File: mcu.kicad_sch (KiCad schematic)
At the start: 32 parts, among them U1 STM32H723VGTx, U13 BMI323, U14 AS5047P-ATST, U15 TCAN1044VDRQ1, X1 8MHz

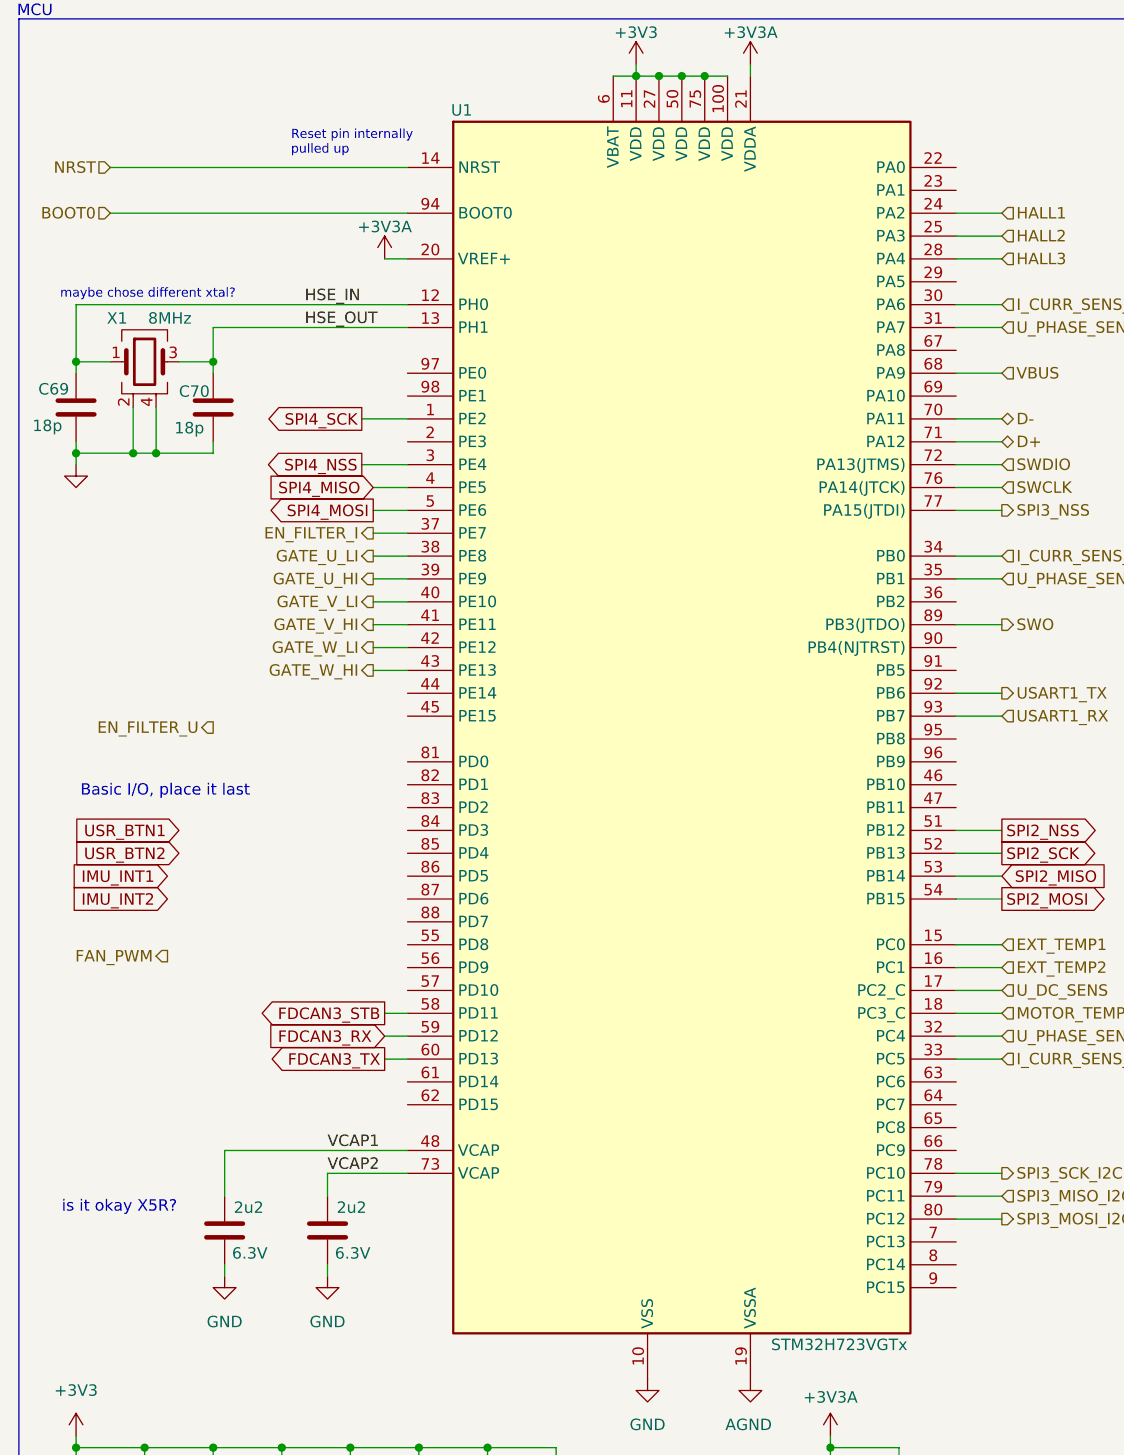
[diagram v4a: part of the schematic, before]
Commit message: added Net Classes  added +5V supply selection header
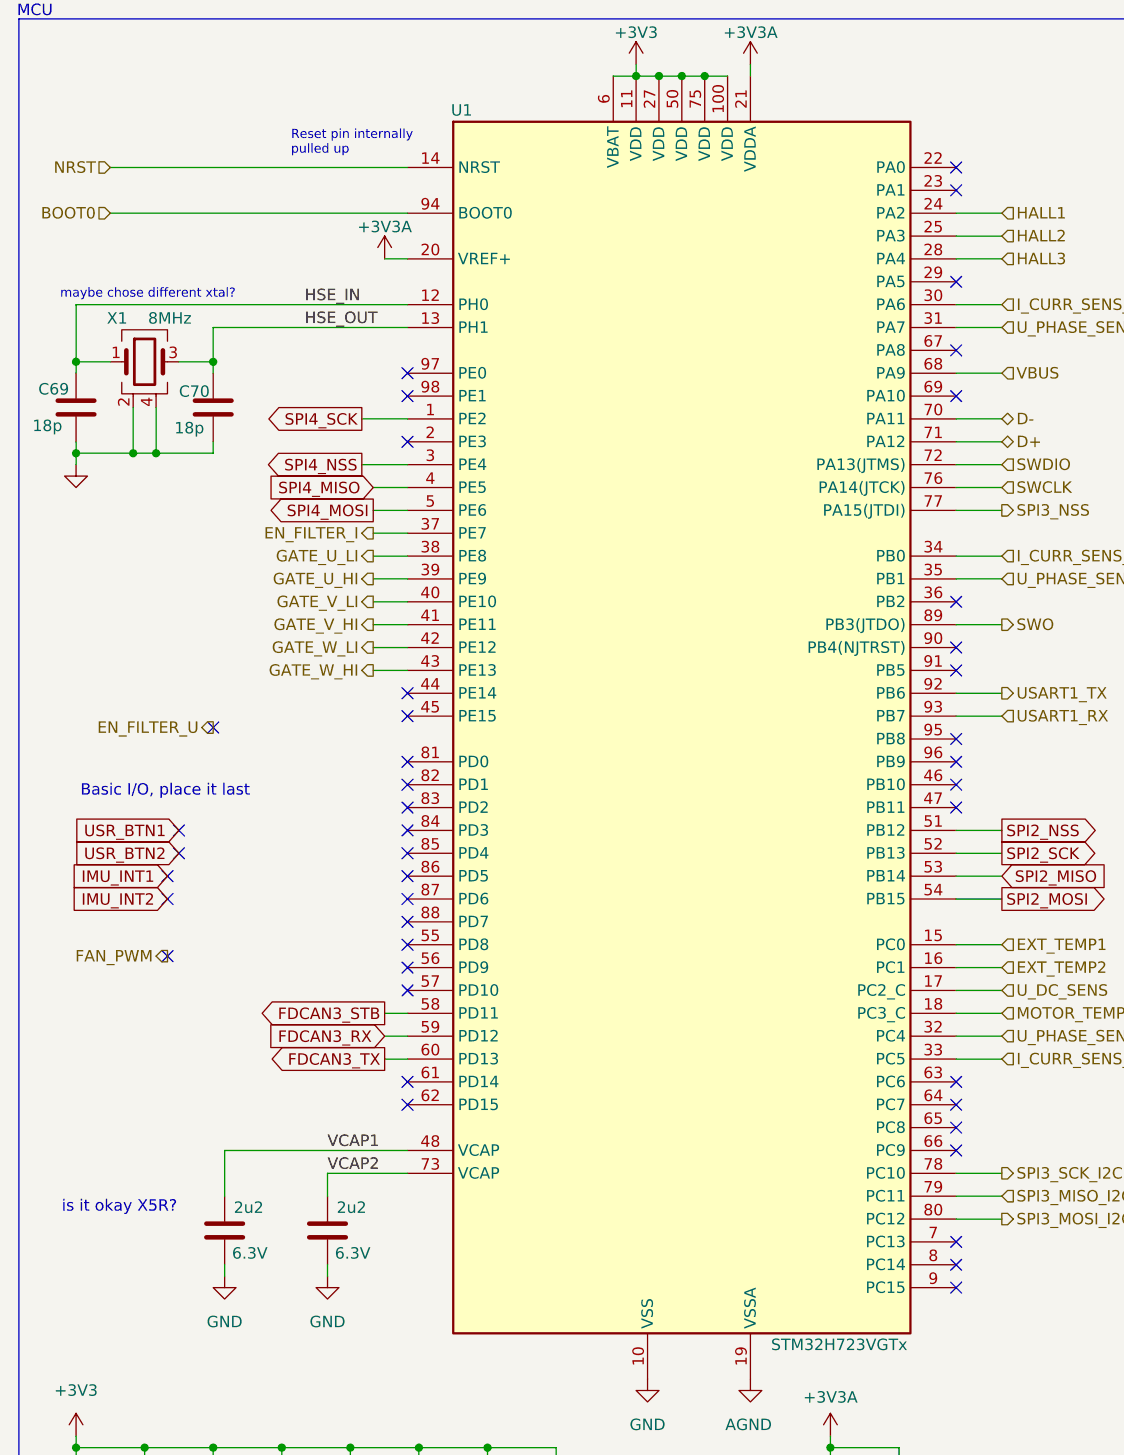
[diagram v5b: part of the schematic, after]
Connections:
- no-connect marks 6 -> 49
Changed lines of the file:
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@@
+	)
+	(no_connect
+		(at 116.84 85.09)
+	)
+	(no_connect
+		(at 116.84 97.79)
+	)
+	(no_connect
+		(at 116.84 133.35)
 	)
 	(no_connect
@@
 	)
 	(no_connect
+		(at 116.84 135.89)
+	)
+	(no_connect
+		(at 116.84 156.21)
+	)
+	(no_connect
+		(at 55.88 97.79)
+	)
+	(no_connect
+		(at 55.88 120.65)
+	)
+	(no_connect
+		(at 55.88 57.15)
+	)
+	(no_connect
+		(at 116.84 100.33)
+	)
+	(no_connect
+		(at 55.88 100.33)
+	)
+	(no_connect
+		(at 55.88 133.35)
+	)
+	(no_connect
+		(at 55.88 107.95)
+	)
+	(no_connect
+		(at 55.88 123.19)
+	)
+	(no_connect
+		(at 116.84 52.07)
+	)
+	(no_connect
 		(at 255.27 69.85)
+	)
+	(no_connect
+		(at 29.21 110.49)
+	)
+	(no_connect
+		(at 55.88 102.87)
+	)
+	(no_connect
+		(at 116.84 140.97)
 	)
 	(no_connect
@@
 	)
 	(no_connect
+		(at 116.84 153.67)
+	)
+	(no_connect
+		(at 55.88 92.71)
+	)
+	(no_connect
+		(at 116.84 95.25)
+	)
+	(no_connect
+		(at 30.48 105.41)
+	)
+	(no_connect
+		(at 55.88 90.17)
+	)
+	(no_connect
+		(at 29.21 113.03)
+	)
+	(no_connect
 		(at 214.63 82.55)
+	)
+	(no_connect
+		(at 116.84 57.15)
+	)
+	(no_connect
+		(at 116.84 102.87)
+	)
+	(no_connect
+		(at 30.48 107.95)
+	)
+	(no_connect
+		(at 34.29 93.98)
+	)
+	(no_connect
+		(at 116.84 44.45)
+	)
+	(no_connect
+		(at 116.84 87.63)
+	)
+	(no_connect
+		(at 55.88 54.61)
 	)
 	(no_connect
@@
 	)
 	(no_connect
+		(at 55.88 62.23)
+	)
+	(no_connect
+		(at 55.88 115.57)
+	)
+	(no_connect
+		(at 116.84 34.29)
+	)
+	(no_connect
+		(at 55.88 113.03)
+	)
+	(no_connect
+		(at 55.88 105.41)
+	)
+	(no_connect
 		(at 255.27 80.01)
 	)
+	(no_connect
+		(at 116.84 31.75)
+	)
+	(no_connect
+		(at 55.88 110.49)
+	)
+	(no_connect
+		(at 55.88 118.11)
+	)
+	(no_connect
+		(at 116.84 80.01)
+	)
+	(no_connect
+		(at 29.21 119.38)
+	)
+	(no_connect
+		(at 116.84 138.43)
+	)
+	(no_connect
+		(at 116.84 151.13)
+	)
+	(no_connect
+		(at 55.88 135.89)
+	)
 	(wire

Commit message: WiP layout
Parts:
- removed R7: 0, Resistor_SMD:R_0402_1005Metric, symbol Device:R_Small
- added C93: 1u, Capacitor_SMD:C_0402_1005Metric, symbol Device:C
- added R7: 10k, Resistor_SMD:R_0402_1005Metric, symbol Device:R
- C69, C70: footprint Capacitor_SMD:C_0603_1608Metric -> Capacitor_SMD:C_0402_1005Metric; LCSC C1647 -> C1549
- C71: value 10u -> 4u7; footprint Capacitor_SMD:C_0805_2012Metric -> Capacitor_SMD:C_0402_1005Metric; LCSC C15850 -> C23733; Voltage Rating 25V -> 10V
- C72: value 1u -> 100n; LCSC C307427 -> C424821
- C79: value 100n -> 1u; LCSC C424821 -> C307427
- R41: footprint Resistor_SMD:R_0603_1608Metric -> Resistor_SMD:R_0402_1005Metric; LCSC C25804 -> C25744
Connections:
- net +3V3: no longer C72.1
- net +3V3A: now also C72.1, C93.1
- net AGND: now also C72.2, C93.2
- net FAN_PWM: now also U1.96 (PB9)
- net GND: now also R7.2; no longer C72.2
- net SPI2_MISO: now also U14.3 (MISO); no longer U13.1 (SDO)
- net SPI2_MOSI: now also U14.4 (MOSI); no longer U13.14 (SDX)
- net SPI2_NSS: now also U14.1 (CSn); no longer U13.12 (CSB)
- net SPI2_SCK: now also U14.2 (CLK); no longer U13.13 (SCX)
- net SPI4_MISO: now also U13.1 (SDO); no longer U14.3 (MISO)
- net SPI4_MOSI: now also U13.14 (SDX); no longer U14.4 (MOSI)
- net SPI4_NSS: now also U13.12 (CSB); no longer U14.1 (CSn)
- net SPI4_SCK: now also U13.13 (SCX); no longer U14.2 (CLK)
- net FDCAN1_RX: now reaches U1.81 (PD0)
- net FDCAN1_RX: now also U15.4 (RXD)
- net FDCAN1_TX: now reaches U1.82 (PD1)
- net FDCAN1_TX: now also U15.1 (TXD)
- net FDCAN1_STB: now reaches U1.83 (PD2)
- net FDCAN1_STB: now also U15.8 (STB), R7.1
- net SERVO: now reaches U1.90 (PB4(NJTRST))
- net SERVO: now also U1.91 (PB5)
- net FDCAN3_RX: no longer names the net of U1.59 (PD12)
- net FDCAN3_RX: no longer U15.4 (RXD)
- net FDCAN3_STB: no longer names the net of U1.58 (PD11)
- net FDCAN3_STB: no longer U15.8 (STB)
- net FDCAN3_TX: no longer names the net of U1.60 (PD13)
- net FDCAN3_TX: no longer U15.1 (TXD)
- no-connect marks 49 -> 45
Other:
- note added: "No RX/TX switch! Double check!"

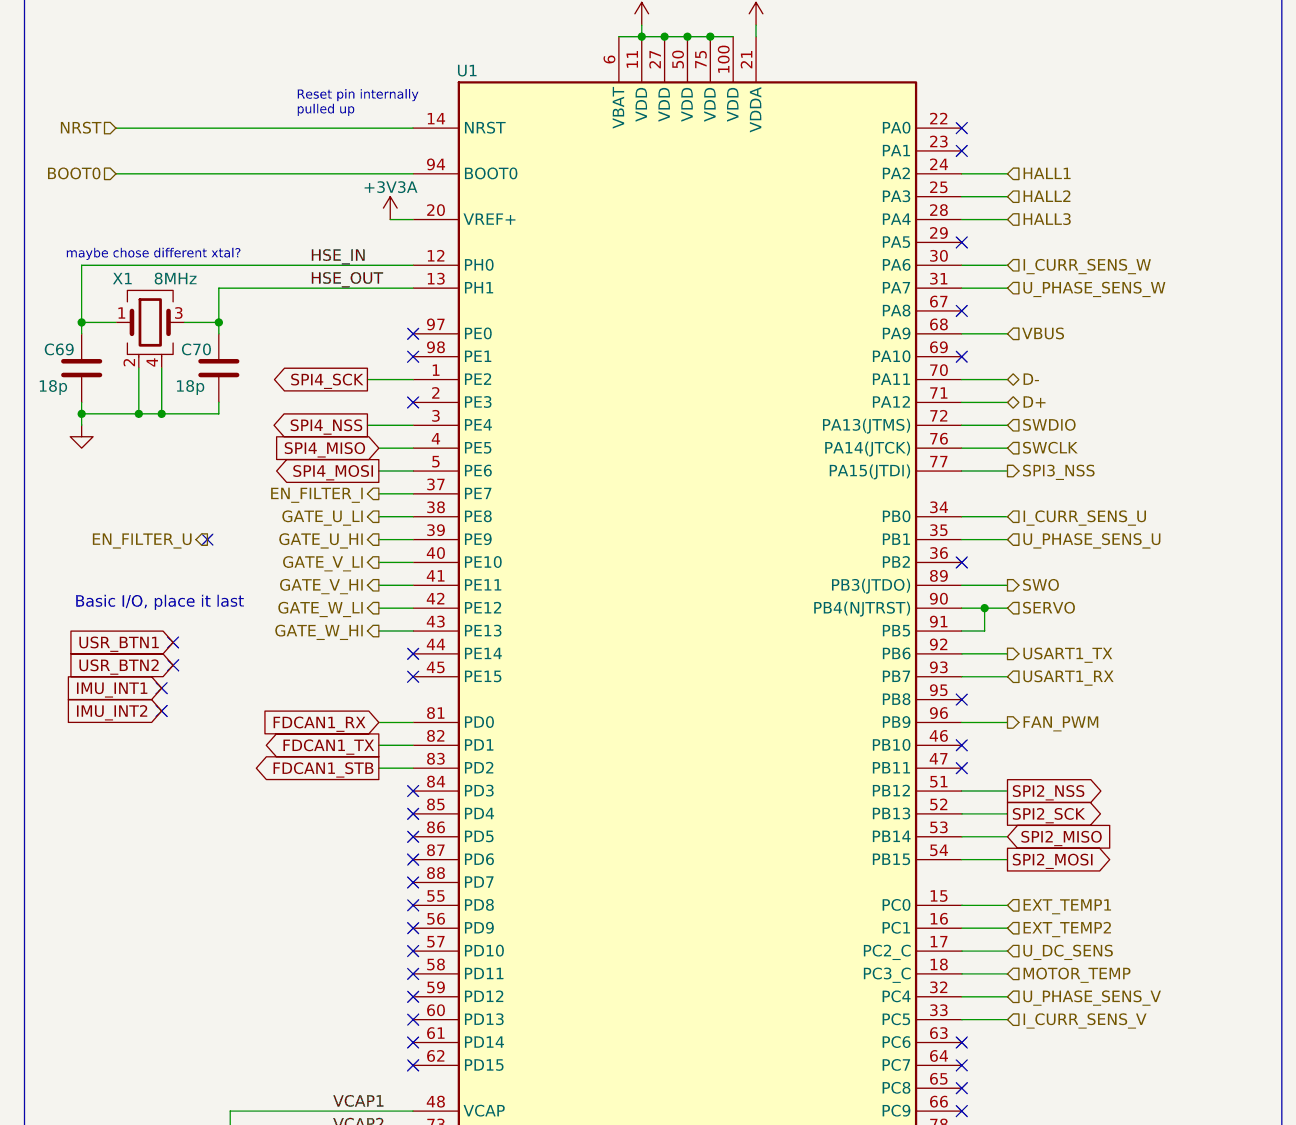
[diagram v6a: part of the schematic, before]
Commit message: added over current protection triggers (adjustable)
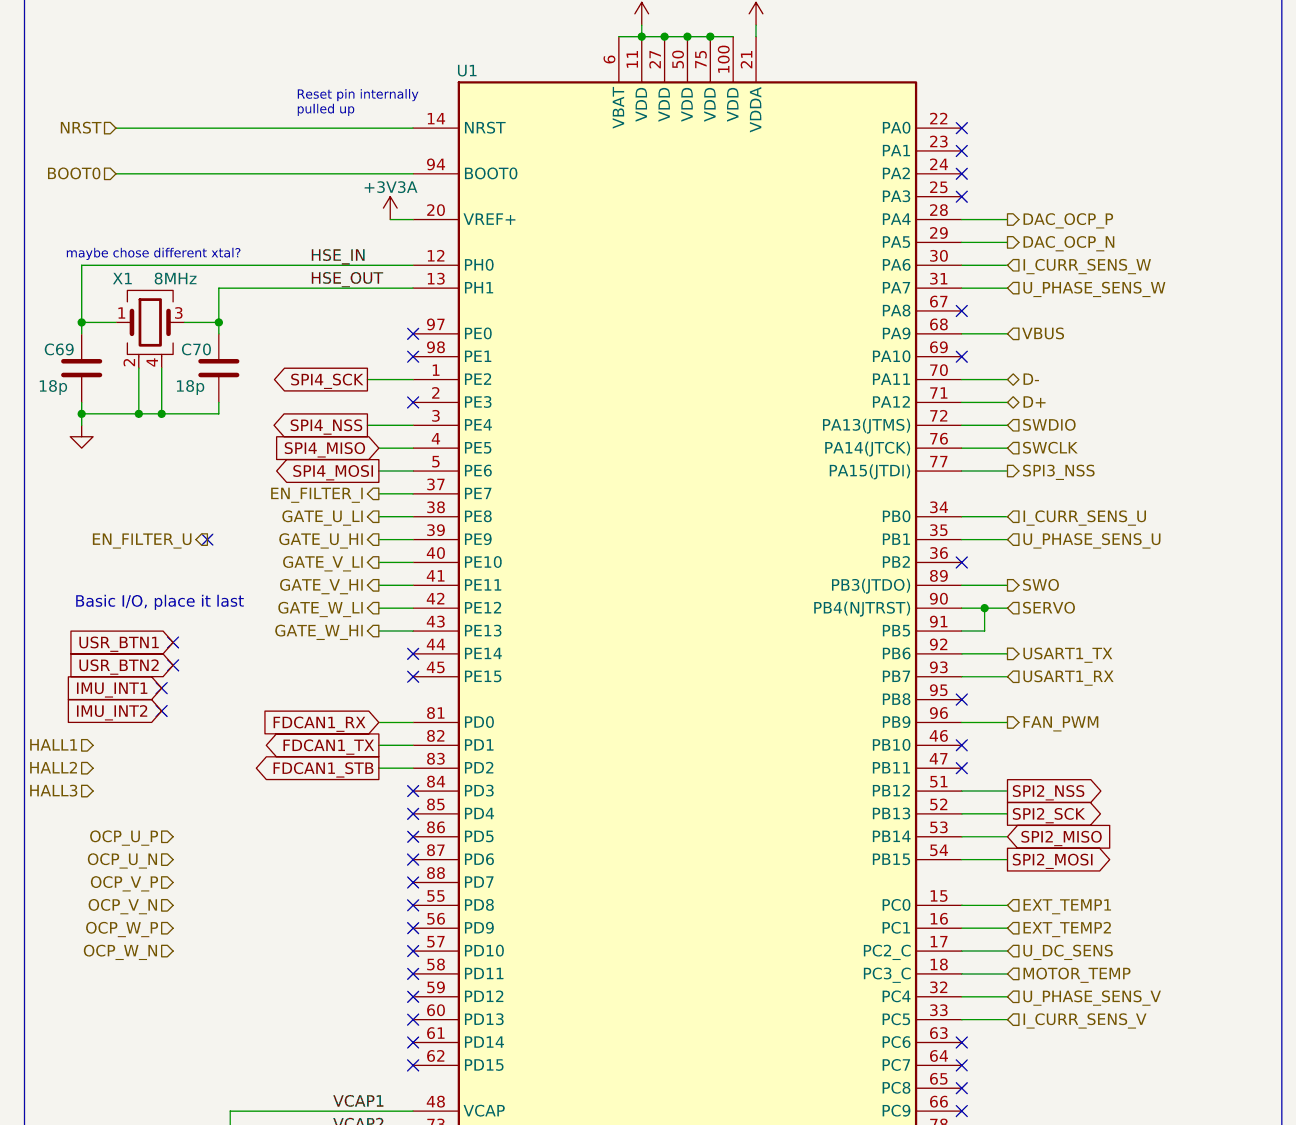
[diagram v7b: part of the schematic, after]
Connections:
- net HALL1: no longer U1.24 (PA2)
- net HALL2: no longer U1.25 (PA3)
- net HALL3: no longer U1.28 (PA4)
- net DAC_OCP_N: now reaches U1.29 (PA5)
- new net DAC_OCP_P: U1.28 (PA4)
- no-connect marks 45 -> 46
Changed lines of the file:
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@@
-	)
-	(no_connect
-		(at 116.84 44.45)
 	)
 	(no_connect
@@
 	)
 	(no_connect
+		(at 116.84 36.83)
+	)
+	(no_connect
 		(at 55.88 113.03)
 	)
@@
 	)
 	(no_connect
+		(at 116.84 39.37)
+	)
+	(no_connect
 		(at 116.84 80.01)
 	)
@@
 	(wire
 		(pts
+			(xy 116.84 41.91) (xy 121.92 41.91)
+		)
+		(stroke
+			(width 0)
+			(type default)
+		)
+	)
+	(wire
+		(pts
 			(xy 116.84 128.27) (xy 121.92 128.27)
 		)
@@
 	(wire
 		(pts
-			(xy 116.84 39.37) (xy 121.92 39.37)
-		)
-		(stroke
-			(width 0)
-			(type default)
-		)
-	)
-	(wire
-		(pts
 			(xy 52.07 85.09) (xy 55.88 85.09)
 		)
@@
 	(wire
 		(pts
-			(xy 116.84 41.91) (xy 121.92 41.91)
-		)
-		(stroke
-			(width 0)
-			(type default)
-		)
-	)
-	(wire
-		(pts
 			(xy 116.84 54.61) (xy 121.92 54.61)
 		)
@@
 	(wire
 		(pts
-			(xy 116.84 36.83) (xy 121.92 36.83)
-		)
-		(stroke
-			(width 0)
-			(type default)
-		)
-	)
-	(wire
-		(pts
 			(xy 252.73 116.84) (xy 255.27 116.84)
 		)
@@
 		(pts
 			(xy 166.37 34.29) (xy 166.37 35.56)
+		)
+		(stroke
+			(width 0)
+			(type default)
+		)
+	)
+	(wire
+		(pts
+			(xy 116.84 44.45) (xy 121.92 44.45)
 		)
 		(stroke
@@
 		)
 	)
+	(hierarchical_label "OCP_V_N"
+		(shape input)
+		(at 29.21 118.11 180)
+		(effects
+			(font
+				(size 1.27 1.27)
+			)
+			(justify right)
+		)
+	)
+	(hierarchical_label "OCP_V_P"
+		(shape input)
+		(at 29.21 115.57 180)
+		(effects
+			(font
+				(size 1.27 1.27)
+			)
+			(justify right)
+		)
+	)
 	(hierarchical_label "NRST"
 		(shape input)
@@
 		)
 	)
+	(hierarchical_label "DAC_OCP_P"
+		(shape output)
+		(at 121.92 41.91 0)
+		(effects
+			(font
+				(size 1.27 1.27)
+			)
+			(justify left)
+		)
+	)
 	(hierarchical_label "HALL1"
 		(shape input)
-		(at 121.92 36.83 0)
-		(effects
-			(font
-				(size 1.27 1.27)
-			)
-			(justify left)
+		(at 20.32 100.33 180)
+		(effects
+			(font
+				(size 1.27 1.27)
+			)
+			(justify right)
 		)
 	)
@@
 		)
 	)
+	(hierarchical_label "OCP_U_N"
+		(shape input)
+		(at 29.21 113.03 180)
+		(effects
+			(font
+				(size 1.27 1.27)
+			)
+			(justify right)
+		)
+	)
+	(hierarchical_label "OCP_U_P"
+		(shape input)
+		(at 29.21 110.49 180)
+		(effects
+			(font
+				(size 1.27 1.27)
+			)
+			(justify right)
+		)
+	)
 	(hierarchical_label "USART1_TX"
 		(shape output)
@@
 		)
 	)
+	(hierarchical_label "DAC_OCP_N"
+		(shape output)
+		(at 121.92 44.45 0)
+		(effects
+			(font
+				(size 1.27 1.27)
+			)
+			(justify left)
+		)
+	)
 	(hierarchical_label "SPI3_MOSI_I2C5_SMBA"
 		(shape output)
@@
 		)
 	)
+	(hierarchical_label "OCP_W_P"
+		(shape input)
+		(at 29.21 120.65 180)
+		(effects
+			(font
+				(size 1.27 1.27)
+			)
+			(justify right)
+		)
+	)
 	(hierarchical_label "HALL3"
 		(shape input)
-		(at 121.92 41.91 0)
-		(effects
-			(font
-				(size 1.27 1.27)
-			)
-			(justify left)
+		(at 20.32 105.41 180)
+		(effects
+			(font
+				(size 1.27 1.27)
+			)
+			(justify right)
 		)
 	)
@@
 	(hierarchical_label "HALL2"
 		(shape input)
-		(at 121.92 39.37 0)
-		(effects
-			(font
-				(size 1.27 1.27)
-			)
-			(justify left)
+		(at 20.32 102.87 180)
+		(effects
+			(font
+				(size 1.27 1.27)
+			)
+			(justify right)
 		)
 	)
@@
 		)
 	)
+	(hierarchical_label "OCP_W_N"
+		(shape input)
+		(at 29.21 123.19 180)
+		(effects
+			(font
+				(size 1.27 1.27)
+			)
+			(justify right)
+		)
+	)
